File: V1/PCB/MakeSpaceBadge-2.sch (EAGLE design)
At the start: 67 parts

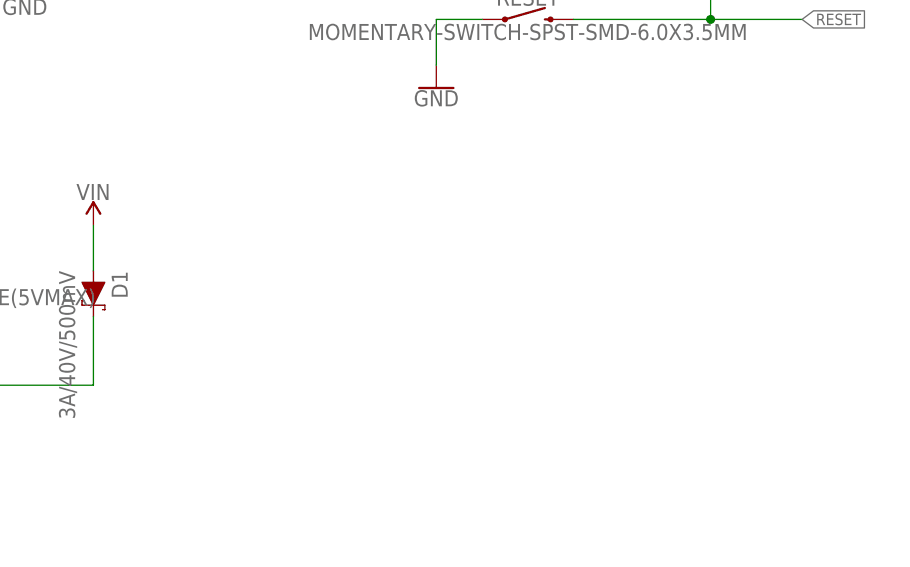
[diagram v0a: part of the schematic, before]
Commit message: Added notes.
Added mini case to hold battery/protect electronics.

Added firmware to drive leds.
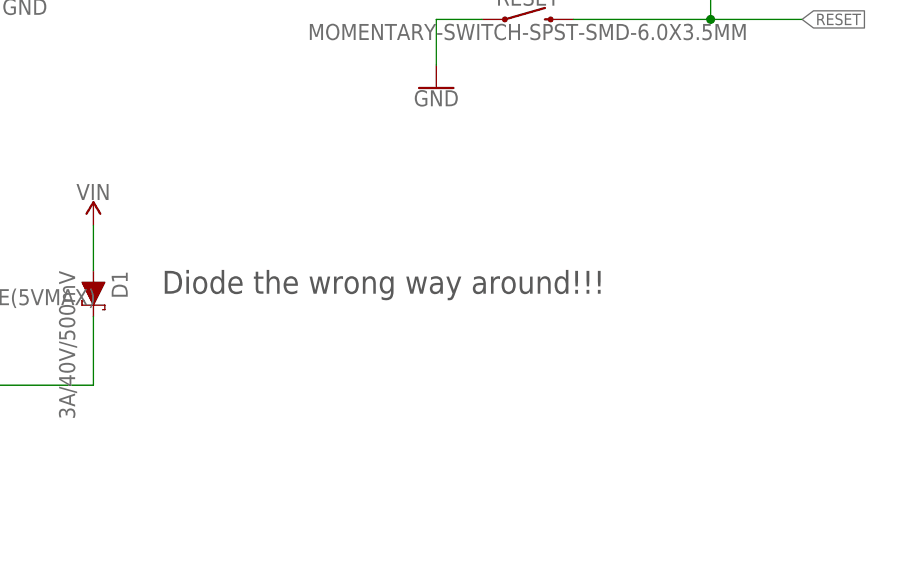
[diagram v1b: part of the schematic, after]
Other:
- note added: "Diode the wrong way around!!!"
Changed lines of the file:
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@@
 <plain>
 <text x="20.32" y="-2.54" size="1.27" layer="91">Power In</text>
+<text x="48.26" y="-7.62" size="2.54" layer="97">Diode the wrong way around!!!</text>
 </plain>
 <instances>
